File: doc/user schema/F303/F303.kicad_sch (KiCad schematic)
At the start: 31 parts

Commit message: f303, f746 uart --implemented
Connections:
- net UART2_RX BT17 renamed UART2_CTS BT17
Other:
- note added: "USB_OTG_FS"
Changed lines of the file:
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@@
     (stroke (width 0) (type default))
+  )
+  (text "USB_OTG_FS" (at 237.49 111.76 0)
+    (effects (font (size 1.27 1.27)) (justify left bottom))
   )
   (text "NUCLEO144-F746ZG-CH7_CH8_CH9_CH10" (at 194.31 29.21 0)
@@
     (effects (font (size 1.27 1.27)) (justify right bottom))
   )
-  (label "UART2_RX BT17" (at 201.93 55.88 0) (fields_autoplaced)
+  (label "UART2_CTS BT17" (at 201.93 55.88 0) (fields_autoplaced)
+    (effects (font (size 1.27 1.27)) (justify left bottom))
+  )
+  (label "PA11(USBOTG_FS_DM)" (at 232.41 119.38 0) (fields_autoplaced)
     (effects (font (size 1.27 1.27)) (justify left bottom))
   )
@@
     (effects (font (size 1.27 1.27)) (justify right bottom))
   )
+  (label "PA8(USB_OTG_FS_SOF)" (at 232.41 114.3 0) (fields_autoplaced)
+    (effects (font (size 1.27 1.27)) (justify left bottom))
+  )
   (label "UART2_RTS R17" (at 144.78 57.15 0) (fields_autoplaced)
     (effects (font (size 1.27 1.27)) (justify left bottom))
@@
   )
   (label "I2C1_SDA Y11" (at 265.43 33.02 0) (fields_autoplaced)
+    (effects (font (size 1.27 1.27)) (justify left bottom))
+  )
+  (label "PA12(USB_OTG_FS_DP)" (at 232.41 121.92 0) (fields_autoplaced)
     (effects (font (size 1.27 1.27)) (justify left bottom))
   )
@@
     (effects (font (size 1.27 1.27)) (justify left bottom))
   )
+  (label "PA9(USB_OTG_FS_VBUS)" (at 232.41 116.84 0) (fields_autoplaced)
+    (effects (font (size 1.27 1.27)) (justify left bottom))
+  )

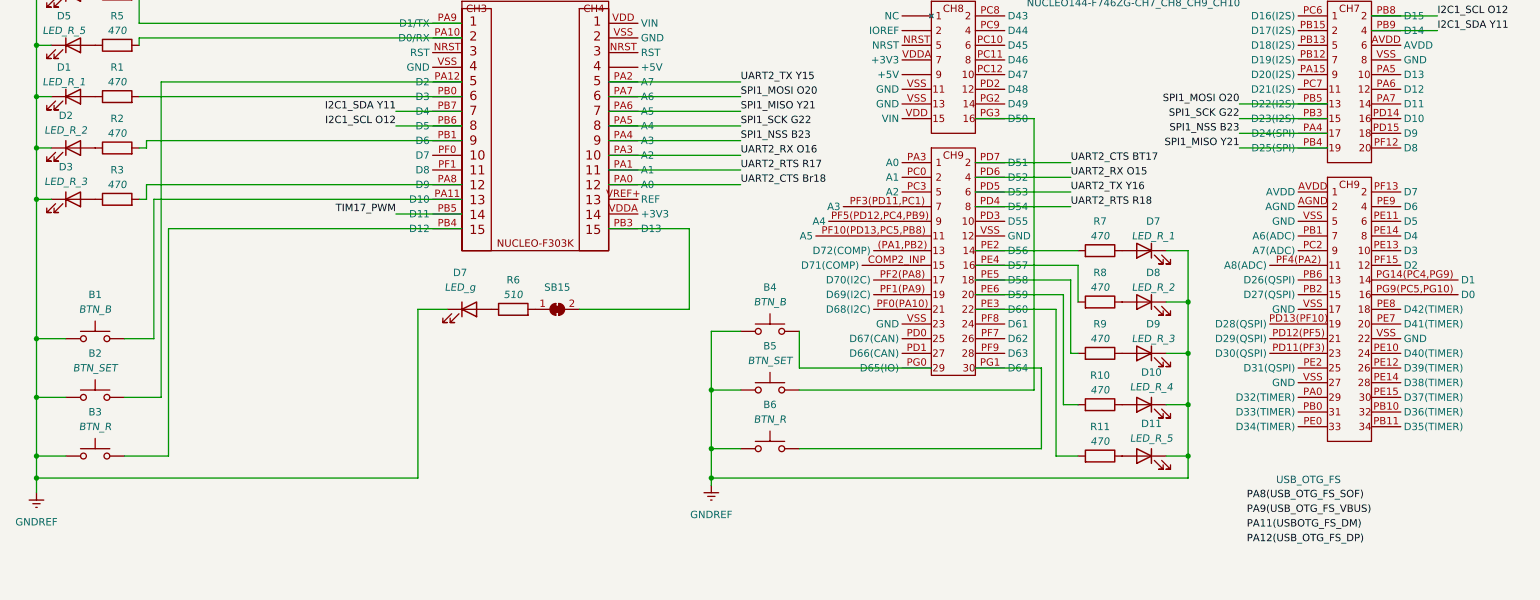
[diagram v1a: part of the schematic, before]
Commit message: Error Handler added
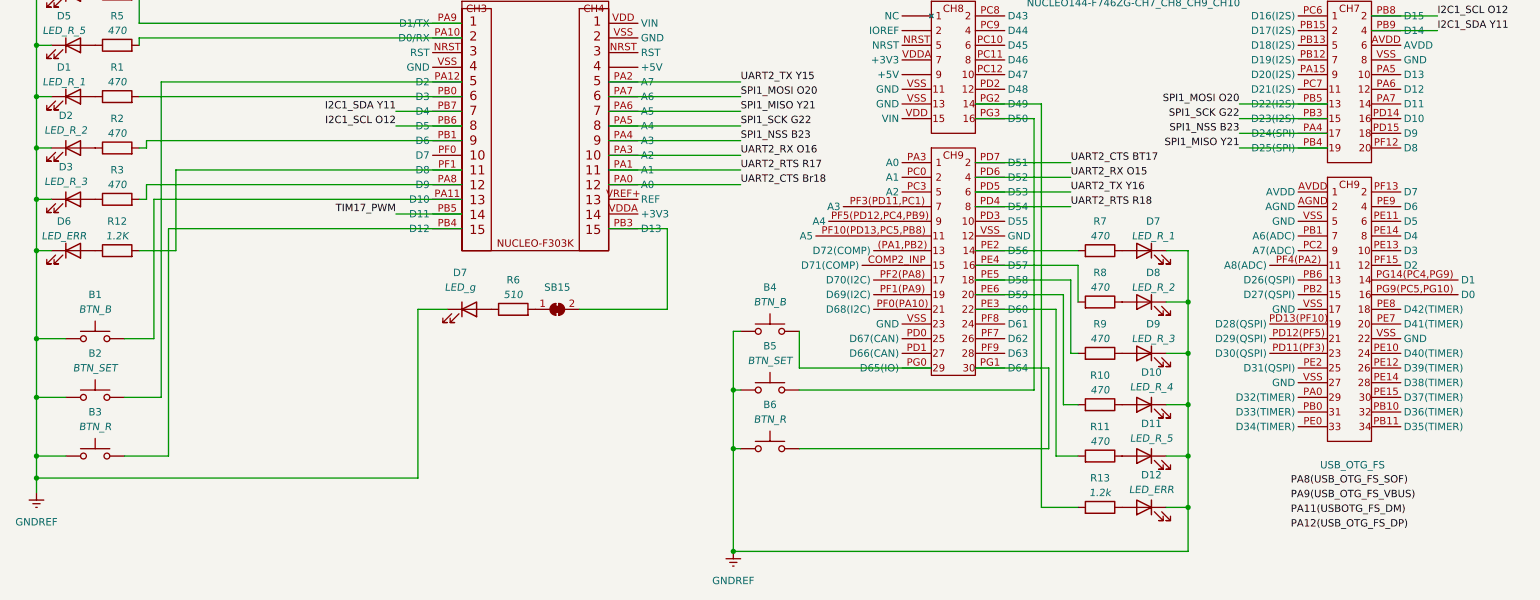
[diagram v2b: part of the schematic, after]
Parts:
- added D12, D6: LED_ERR, symbol Device:LED
- added R12: 1.2K, symbol Device:R
- added R13: 1.2k, symbol Device:R
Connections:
- net GNDREF: now also D12.1 (K), D6.1 (K)
- net at U1.PF1 (D8): now also R12.2
- net at U2.PG2 (D49): now also R13.2
- new net: D6.2 (A), R12.1
- new net: D12.2 (A), R13.1

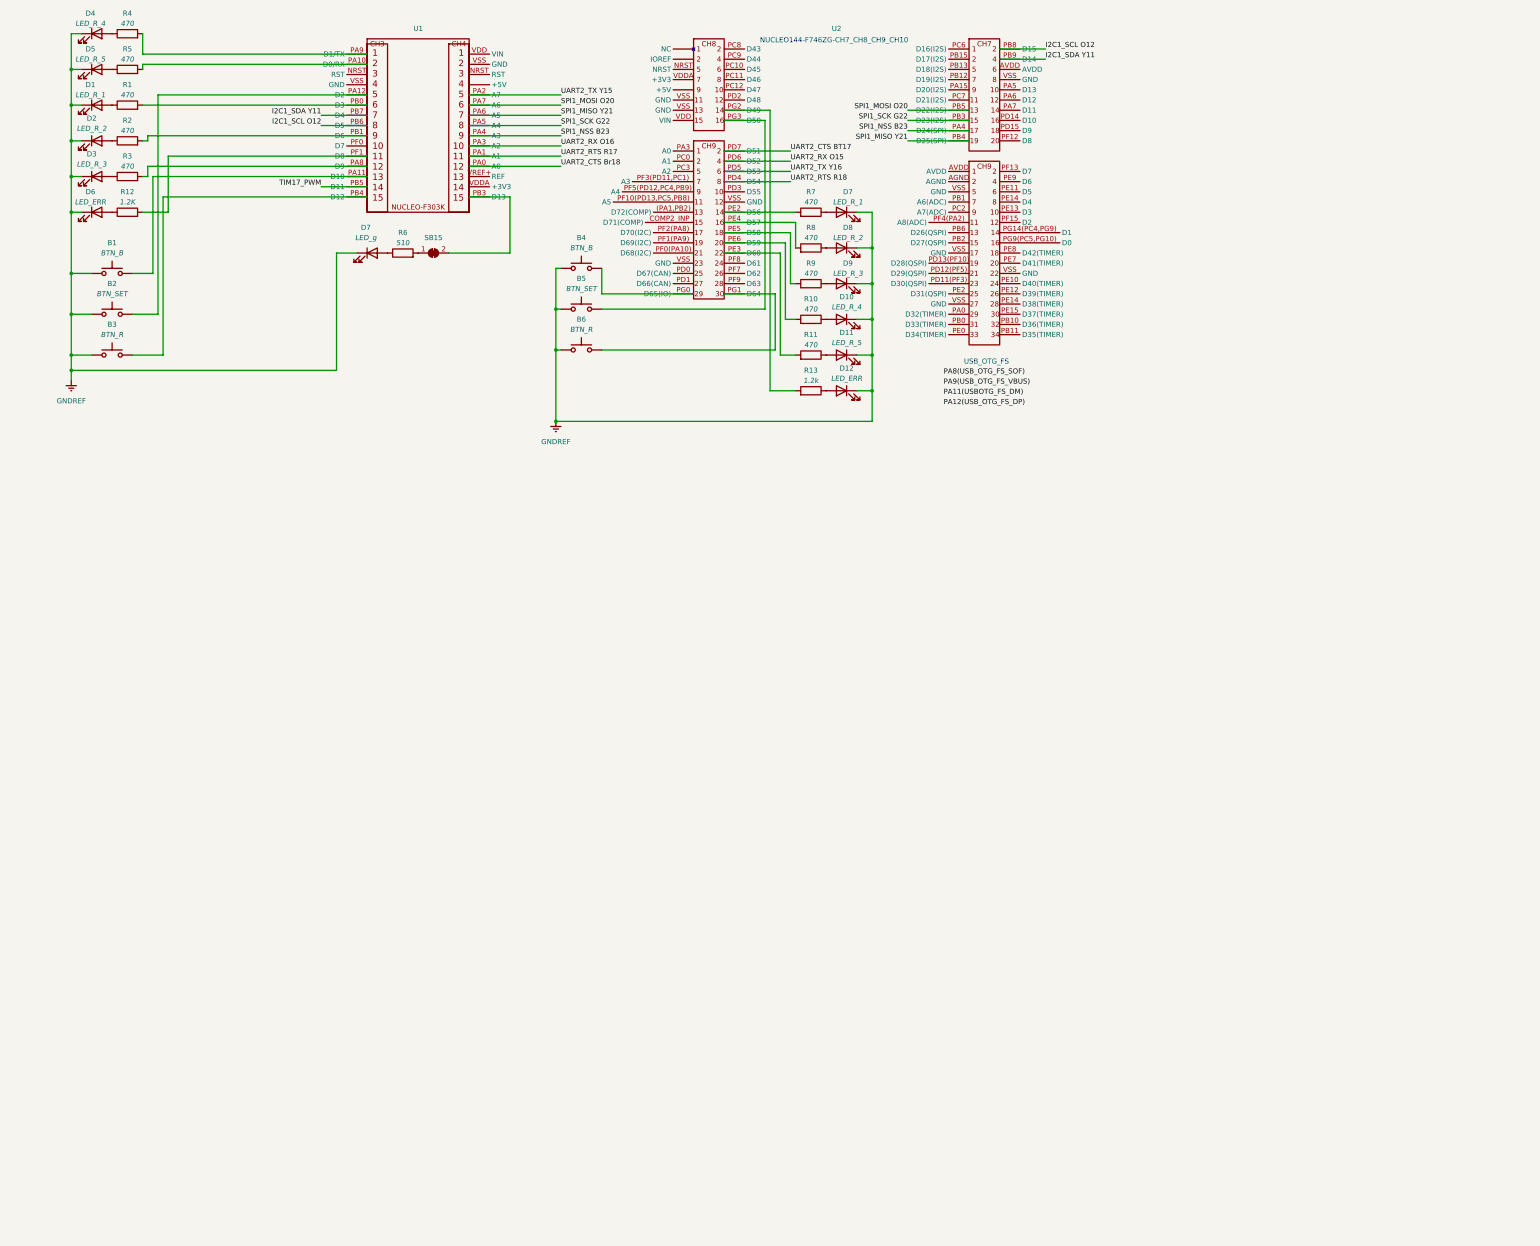
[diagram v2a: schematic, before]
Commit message: spi connection added
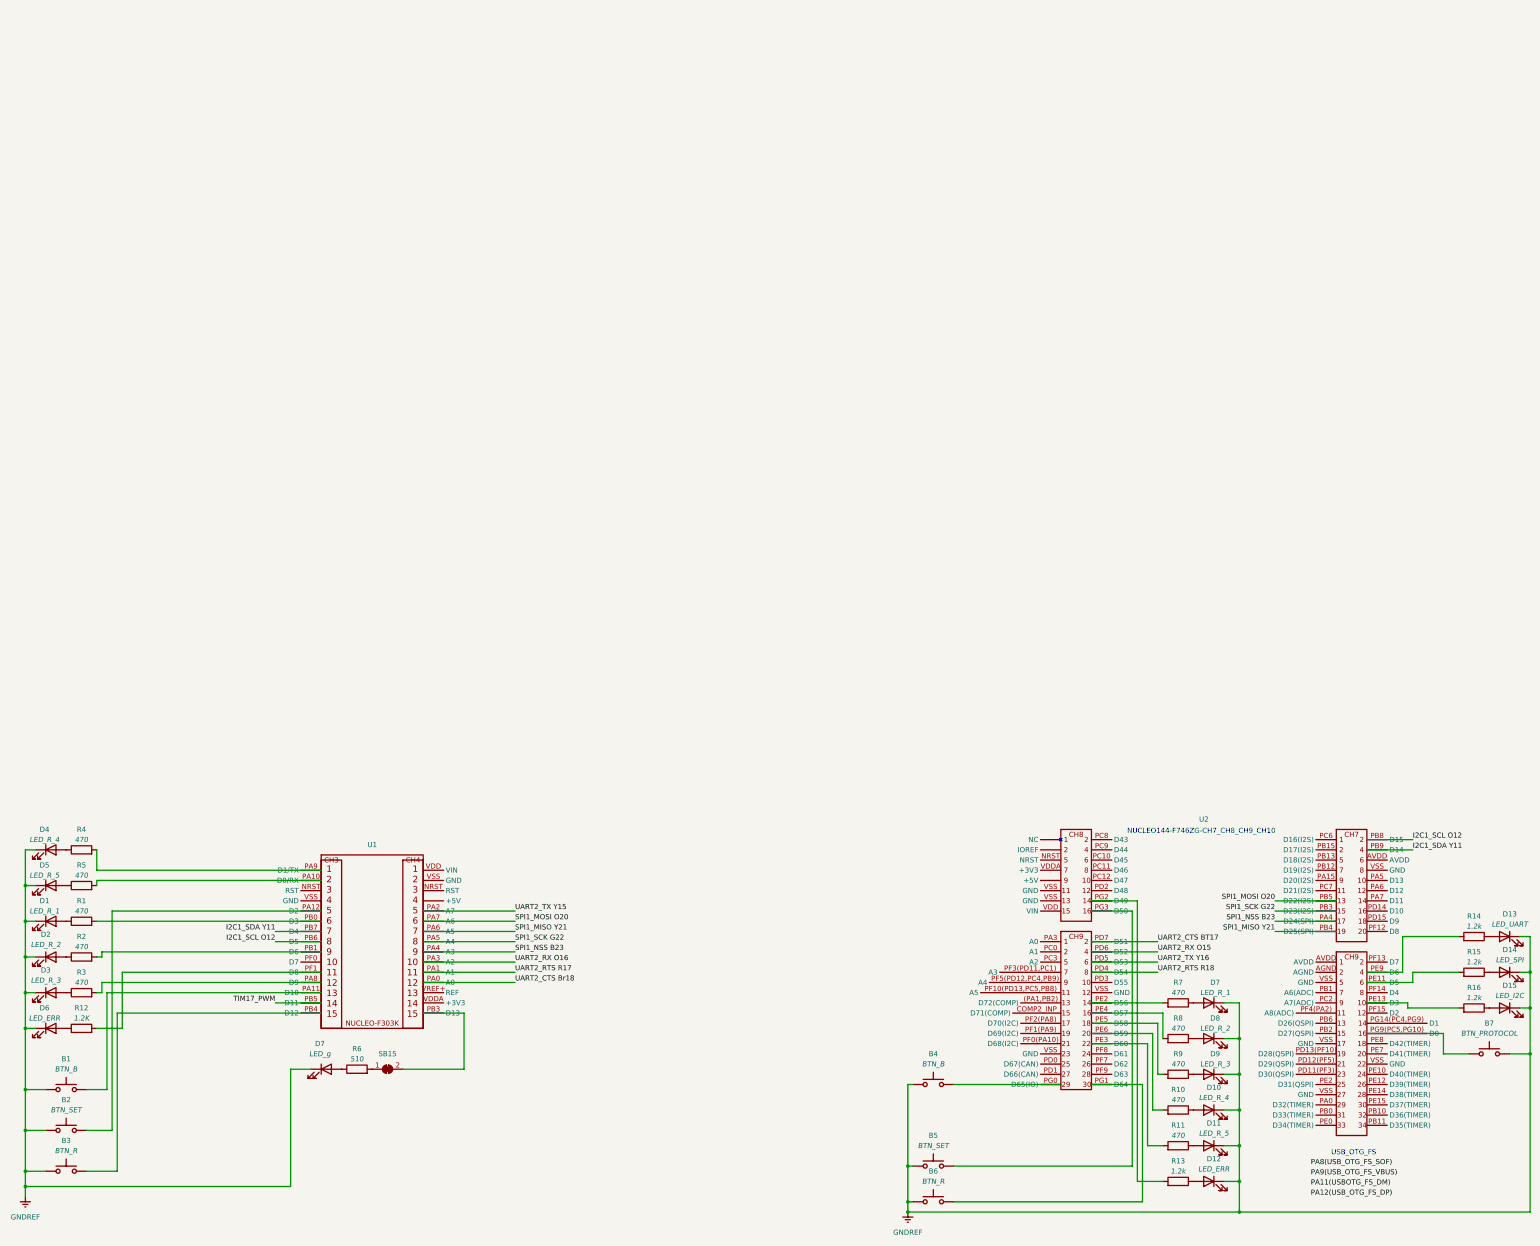
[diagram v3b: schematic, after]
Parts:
- added B7: BTN_PROTOCOL, symbol Switch:SW_Push
- added D13: LED_UART, symbol Device:LED
- added D14: LED_SPI, symbol Device:LED
- added D15: LED_I2C, symbol Device:LED
- added R14, R15, R16: 1.2k, symbol Device:R
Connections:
- net GNDREF: now also B7.2, D13.1 (K), D14.1 (K), D15.1 (K)
- net at U2.PE11 (D5): now also R15.2
- net at U2.PE13 (D3): now also R16.2
- net at U2.PE9 (D6): now also R14.2
- net at U2.PG9(PC5,PG10) (D0): now also B7.1
- new net: D15.2 (A), R16.1
- new net: D13.2 (A), R14.1
- new net: D14.2 (A), R15.1
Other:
- moved on the sheet: B1, B2, B3, B4, B5, B6, D1, D10, D11, D12, D2, D3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

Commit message: registers of 303 project started
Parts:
- added R17, R18, R19, R20: 10k, symbol Device:R
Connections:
- net I2C1_SCL O12: no longer U1.PB6 (D5)
- net I2C1_SDA Y11: no longer U1.PB7 (D4)
- net SPI1_MISO Y21: no longer U1.PA6 (A5)
- net SPI1_MOSI O20: no longer U1.PA7 (A6)
- net SPI1_SCK G22: no longer U1.PA5 (A4)
- net +5V: now reaches U1. (+5V)
- net +5V: now also R17.1, R18.1, R19.1, R20.1
- net at U1.NRST (RST): now also R17.2
- net at U2.NRST: now also R18.2
- net SPI_NSS_OUT V12: now reaches U2.PC7 (D21(I2S))
- net SPI1_NSS B23 renamed SPI1_NSS B13
- net SPI1_NSS B13: no longer U1.PA4 (A3)
- net TIM17_PWM renamed SPI_NSS_OUT V13
- net UART2_CTS Br18 renamed UART2_CTS Br7
- net UART2_RTS R17 renamed UART2_RTS R6
- net UART2_RX O16 renamed UART2_RX O5
- net UART2_TX Y15 renamed UART2_TX Y4
- new net I2C1_SCL O2: U1.PB6 (D5)
- new net I2C1_SDA Y1: U1.PB7 (D4)
- new net SPI1_MISO Y11: U1.PA6 (A5)
- new net SPI1_MOSI O9: U1.PA7 (A6)
- new net SPI1_NSS_IN B12: R19.2, R20.2
- new net SPI1_NSS_IN B13: U1.PA4 (A3)
- new net SPI1_SCK G12: U1.PA5 (A4)
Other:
- note added: "STM SPI CONNECTION MASTER-SLAVE"
